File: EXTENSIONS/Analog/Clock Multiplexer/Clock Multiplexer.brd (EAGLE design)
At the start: 68 x 71 mm, 19 parts

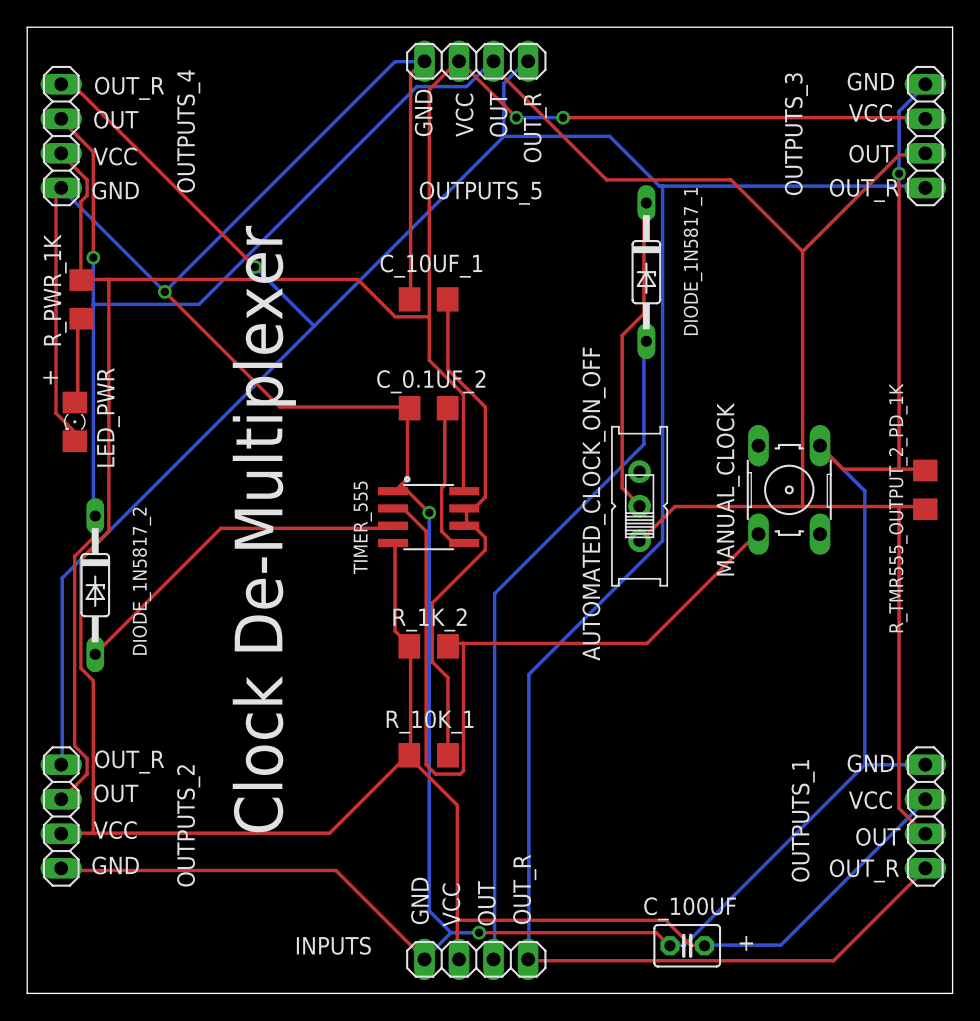
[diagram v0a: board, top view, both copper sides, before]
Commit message: Add pull up resistor to ft232h and i2c out 2
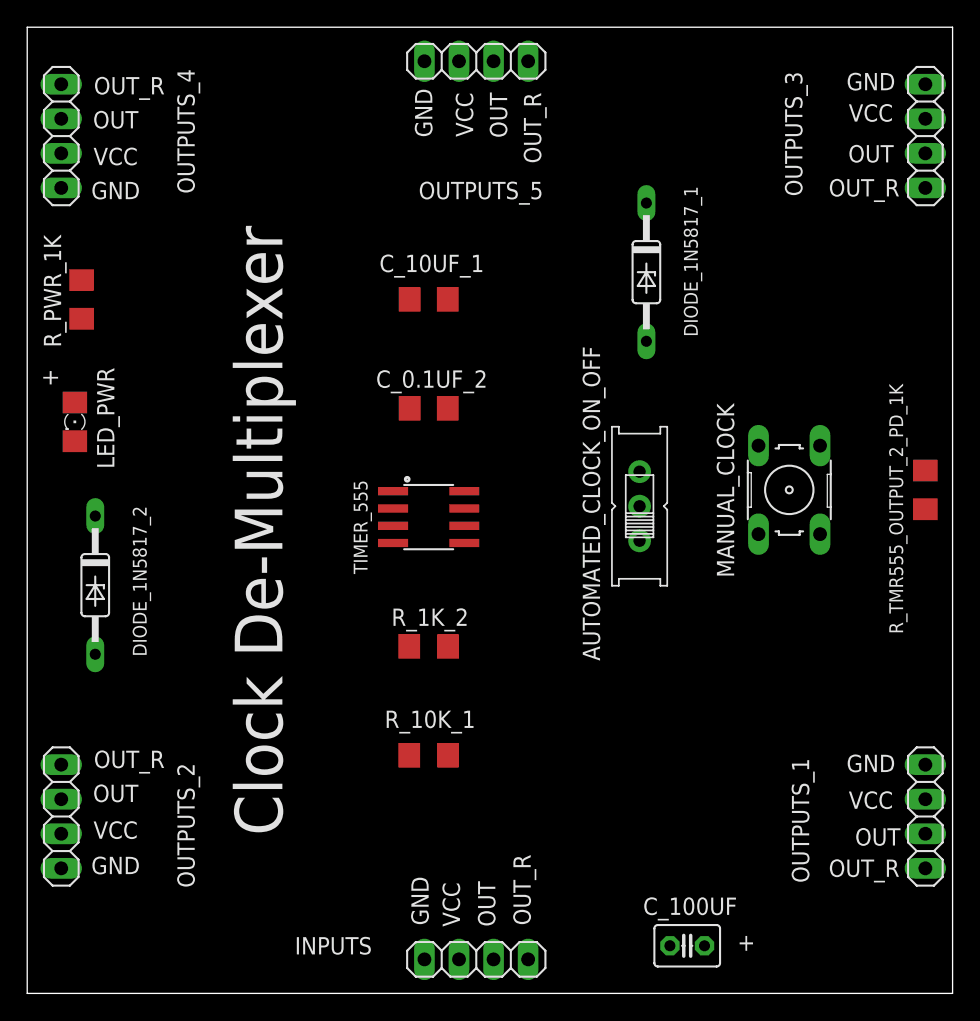
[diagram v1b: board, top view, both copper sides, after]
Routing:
- net GND: track 272.3 -> 0.00 mm, vias 4 -> 0
- net VCC: track 248.9 -> 0.00 mm, vias 2 -> 0
- net TMR555_OUTPUT_REVERSE: track 217.5 -> 0.00 mm, vias 1 -> 0
- net TMR555_OUTPUT_2: track 196.3 -> 0.00 mm, vias 1 -> 0
- net N$5: track 59.0 -> 0.00 mm
- net TMR555_OUTPUT: track 50.1 -> 0.00 mm
- net N$3: track 39.1 -> 0.00 mm
- net TIMER_OUTPUT: track 25.9 -> 0.00 mm
- net N$2: track 23.6 -> 0.00 mm
- net N$4: track 11.3 -> 0.00 mm
- net N$1: track 6.39 -> 0.00 mm
